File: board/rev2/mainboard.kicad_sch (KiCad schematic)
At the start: 0 parts

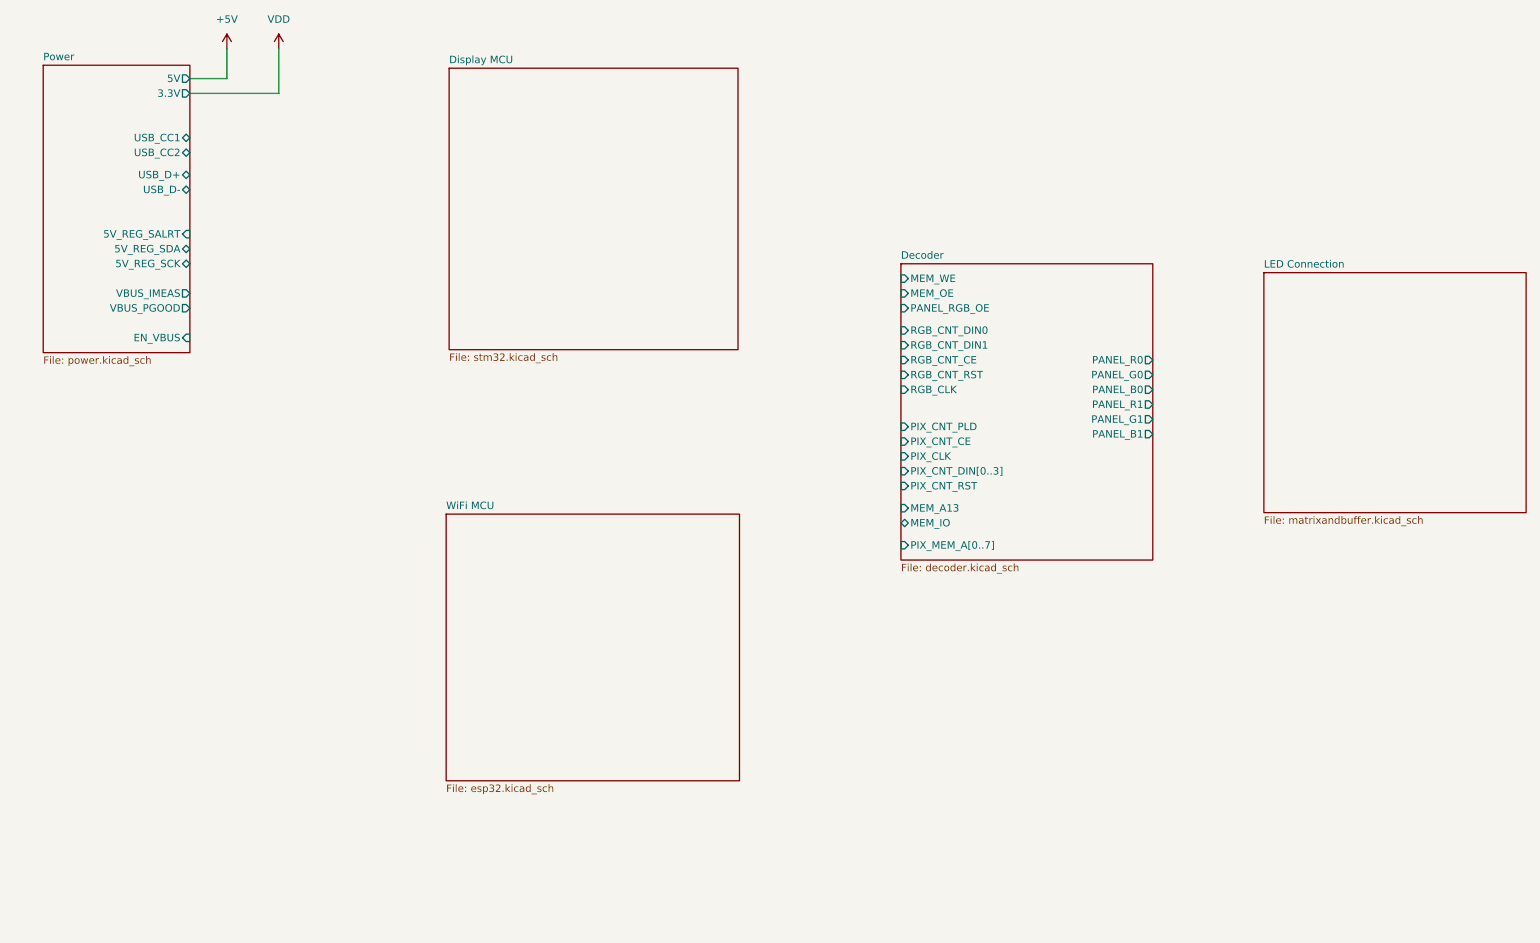
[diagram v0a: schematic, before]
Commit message: Continue board work
- move to rp2040, separate stm32g071 to do usb-c + aux ctrl IO
  - still cheaper lol with the cost of stm32s
- more power reg stuff
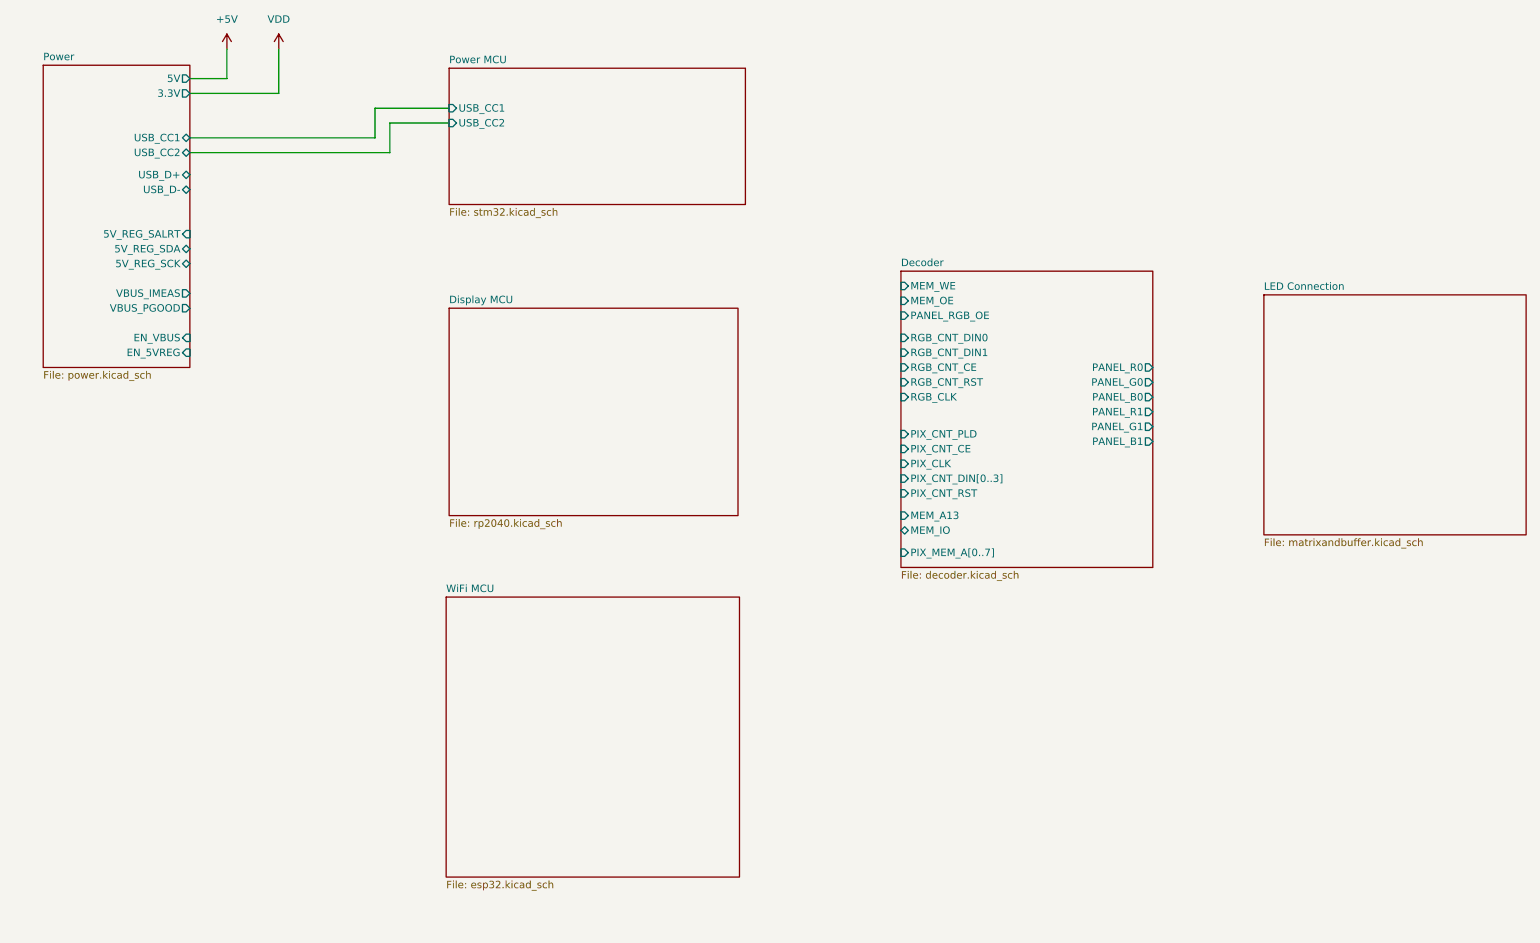
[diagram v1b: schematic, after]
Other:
- added sheet Power MCU (stm32.kicad_sch)
- sheet Display MCU: file stm32.kicad_sch -> rp2040.kicad_sch
- sheet Power ports: added EN_5VREG; removed none
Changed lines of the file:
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@@
+	(wire
+		(pts
+			(xy 80.01 39.37) (xy 45.72 39.37)
+		)
+		(stroke
+			(width 0)
+			(type default)
+		)
+	)
+	(wire
+		(pts
+			(xy 77.47 36.83) (xy 77.47 31.75)
+		)
+		(stroke
+			(width 0)
+			(type default)
+		)
+	)
 	(wire
 		(pts
@@
 	(wire
 		(pts
+			(xy 77.47 31.75) (xy 90.17 31.75)
+		)
+		(stroke
+			(width 0)
+			(type default)
+		)
+	)
+	(wire
+		(pts
 			(xy 45.72 26.67) (xy 52.07 26.67)
 		)
@@
 	(wire
 		(pts
+			(xy 90.17 34.29) (xy 80.01 34.29)
+		)
+		(stroke
+			(width 0)
+			(type default)
+		)
+	)
+	(wire
+		(pts
 			(xy 52.07 26.67) (xy 52.07 21.59)
+		)
+		(stroke
+			(width 0)
+			(type default)
+		)
+	)
+	(wire
+		(pts
+			(xy 45.72 36.83) (xy 77.47 36.83)
+		)
+		(stroke
+			(width 0)
+			(type default)
+		)
+	)
+	(wire
+		(pts
+			(xy 80.01 34.29) (xy 80.01 39.37)
 		)
 		(stroke
@@
 	)
 	(sheet
-		(at 167.64 58.42)
+		(at 90.17 66.04)
+		(size 49.53 35.56)
+		(exclude_from_sim no)
+		(in_bom yes)
+		(on_board yes)
+		(dnp no)
+		(fields_autoplaced yes)
+		(stroke
+			(width 0.1524)
+			(type solid)
+		)
+		(fill
+			(color 0 0 0 0.0000)
+		)
+		(property "Sheetname" "Display MCU"
+			(at 90.17 65.3284 0)
+			(effects
+				(font
+					(size 1.27 1.27)
+				)
+				(justify left bottom)
+			)
+		)
+		(property "Sheetfile" "rp2040.kicad_sch"
+			(at 90.17 102.1846 0)
+			(effects
+				(font
+					(size 1.27 1.27)
+				)
+				(justify left top)
+			)
+		)
+		(instances
+			(project "mainboard"
+				(path "/32eb05c7-b4a6-42f3-8fb3-43453631100f"
+					(page "7")
+				)
+			)
+		)
+	)
+	(sheet
+		(at 167.64 59.69)
 		(size 43.18 50.8)
 		(exclude_from_sim no)
@@
 		)
 		(property "Sheetname" "Decoder"
-			(at 167.64 57.7084 0)
+			(at 167.64 58.9784 0)
 			(effects
 				(font
@@
 		)
 		(property "Sheetfile" "decoder.kicad_sch"
-			(at 167.64 109.8046 0)
+			(at 167.64 111.0746 0)
 			(effects
 				(font
@@
 		)
 		(pin "MEM_WE" input
-			(at 167.64 60.96 180)
+			(at 167.64 62.23 180)
 			(effects
 				(font
@@
 		)
 		(pin "MEM_OE" input
-			(at 167.64 63.5 180)
+			(at 167.64 64.77 180)
 			(effects
 				(font
@@
 		)
 		(pin "PANEL_RGB_OE" input
-			(at 167.64 66.04 180)
+			(at 167.64 67.31 180)
 			(effects
 				(font
@@
 		)
 		(pin "RGB_CNT_DIN0" input
-			(at 167.64 69.85 180)
+			(at 167.64 71.12 180)
 			(effects
 				(font
@@
 		)
 		(pin "RGB_CNT_DIN1" input
-			(at 167.64 72.39 180)
+			(at 167.64 73.66 180)
 			(effects
 				(font
@@
 		)
 		(pin "RGB_CNT_CE" input
-			(at 167.64 74.93 180)
+			(at 167.64 76.2 180)
 			(effects
 				(font
@@
 		)
 		(pin "RGB_CNT_RST" input
-			(at 167.64 77.47 180)
+			(at 167.64 78.74 180)
 			(effects
 				(font
@@
 		)
 		(pin "RGB_CLK" input
-			(at 167.64 80.01 180)
+			(at 167.64 81.28 180)
 			(effects
 				(font
@@
 		)
 		(pin "PIX_CNT_PLD" input
-			(at 167.64 86.36 180)
+			(at 167.64 87.63 180)
 			(effects
 				(font
@@
 		)
 		(pin "PIX_CNT_CE" input
-			(at 167.64 88.9 180)
+			(at 167.64 90.17 180)
 			(effects
 				(font
@@
 		)
 		(pin "PIX_CLK" input
-			(at 167.64 91.44 180)
+			(at 167.64 92.71 180)
 			(effects
 				(font
@@
 		)
 		(pin "PIX_CNT_DIN[0..3]" input
-			(at 167.64 93.98 180)
+			(at 167.64 95.25 180)
 			(effects
 				(font
@@
 		)
 		(pin "PIX_CNT_RST" input
-			(at 167.64 96.52 180)
+			(at 167.64 97.79 180)
 			(effects
 				(font
@@
 		)
 		(pin "PANEL_B1" output
-			(at 210.82 87.63 0)
+			(at 210.82 88.9 0)
 			(effects
 				(font
@@
 		)
 		(pin "PANEL_G0" output
-			(at 210.82 77.47 0)
+			(at 210.82 78.74 0)
 			(effects
 				(font
@@
 		)
 		(pin "PANEL_R0" output
-			(at 210.82 74.93 0)
+			(at 210.82 76.2 0)
 			(effects
 				(font
@@
 		)
 		(pin "PANEL_G1" output
-			(at 210.82 85.09 0)
+			(at 210.82 86.36 0)
 			(effects
 				(font
@@
 		)
 		(pin "PANEL_R1" output
-			(at 210.82 82.55 0)
+			(at 210.82 83.82 0)
 			(effects
 				(font
@@
 		)
 		(pin "PANEL_B0" output
-			(at 210.82 80.01 0)
+			(at 210.82 81.28 0)
 			(effects
 				(font
@@
 		)
 		(pin "MEM_A13" input
-			(at 167.64 100.33 180)
+			(at 167.64 101.6 180)
 			(effects
 				(font
@@
 		)
 		(pin "MEM_IO" bidirectional
-			(at 167.64 102.87 180)
+			(at 167.64 104.14 180)
 			(effects
 				(font
@@
 		)
 		(pin "PIX_MEM_A[0..7]" input
-			(at 167.64 106.68 180)
+			(at 167.64 107.95 180)
 			(effects
 				(font
@@
 	(sheet
 		(at 90.17 24.892)
-		(size 49.53 48.26)
+		(size 50.8 23.368)
 		(exclude_from_sim no)
 		(in_bom yes)
@@
 			(color 0 0 0 0.0000)
 		)
-		(property "Sheetname" "Display MCU"
+		(property "Sheetname" "Power MCU"
 			(at 90.17 24.1804 0)
 			(effects
@@
 		)
 		(property "Sheetfile" "stm32.kicad_sch"
-			(at 90.17 73.7366 0)
+			(at 90.17 48.8446 0)
 			(effects
 				(font
@@
 				)
 				(justify left top)
+			)
+		)
+		(pin "USB_CC1" input
+			(at 90.17 31.75 180)
+			(effects
+				(font
+					(size 1.27 1.27)
+				)
+				(justify left)
+			)
+		)
+		(pin "USB_CC2" input
+			(at 90.17 34.29 180)
+			(effects
+				(font
+					(size 1.27 1.27)
+				)
+				(justify left)
 			)
 		)
@@
 	(sheet
 		(at 20.574 24.384)
-		(size 25.146 49.276)
+		(size 25.146 51.816)
 		(exclude_from_sim no)
 		(in_bom yes)
@@
 		)
 		(property "Sheetfile" "power.kicad_sch"
-			(at 20.574 74.2446 0)
+			(at 20.574 76.7846 0)
 			(effects
 				(font
@@
 		(pin "VBUS_PGOOD" output
 			(at 45.72 66.04 0)
+			(effects
+				(font
+					(size 1.27 1.27)
+				)
+				(justify right)
+			)
+		)
+		(pin "EN_5VREG" input
+			(at 45.72 73.66 0)
 			(effects
 				(font
@@
 	)
 	(sheet
-		(at 89.662 101.346)
-		(size 50.292 45.72)
+		(at 89.662 115.57)
+		(size 50.292 48.006)
 		(exclude_from_sim no)
 		(in_bom yes)
@@
 		)
 		(property "Sheetname" "WiFi MCU"
-			(at 89.662 100.6344 0)
+			(at 89.662 114.8584 0)
 			(effects
 				(font
@@
 		)
 		(property "Sheetfile" "esp32.kicad_sch"
-			(at 89.662 147.6506 0)
+			(at 89.662 164.1606 0)
 			(effects
 				(font
@@
 	)
 	(sheet
-		(at 229.87 59.944)
+		(at 229.87 63.754)
 		(size 44.958 41.148)
 		(exclude_from_sim no)
@@
 		)
 		(property "Sheetname" "LED Connection"
-			(at 229.87 59.2324 0)
+			(at 229.87 63.0424 0)
 			(effects
 				(font
@@
 		)
 		(property "Sheetfile" "matrixandbuffer.kicad_sch"
-			(at 229.87 101.6766 0)
+			(at 229.87 105.4866 0)
 			(effects
 				(font
@@
 			(project "mainboard"
 				(path "/32eb05c7-b4a6-42f3-8fb3-43453631100f"
-					(page "7")
-				)
-			)
+					(page "9")
+				)
+			)

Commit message: Split out board into A/B
allow 2x displays (for chaining)
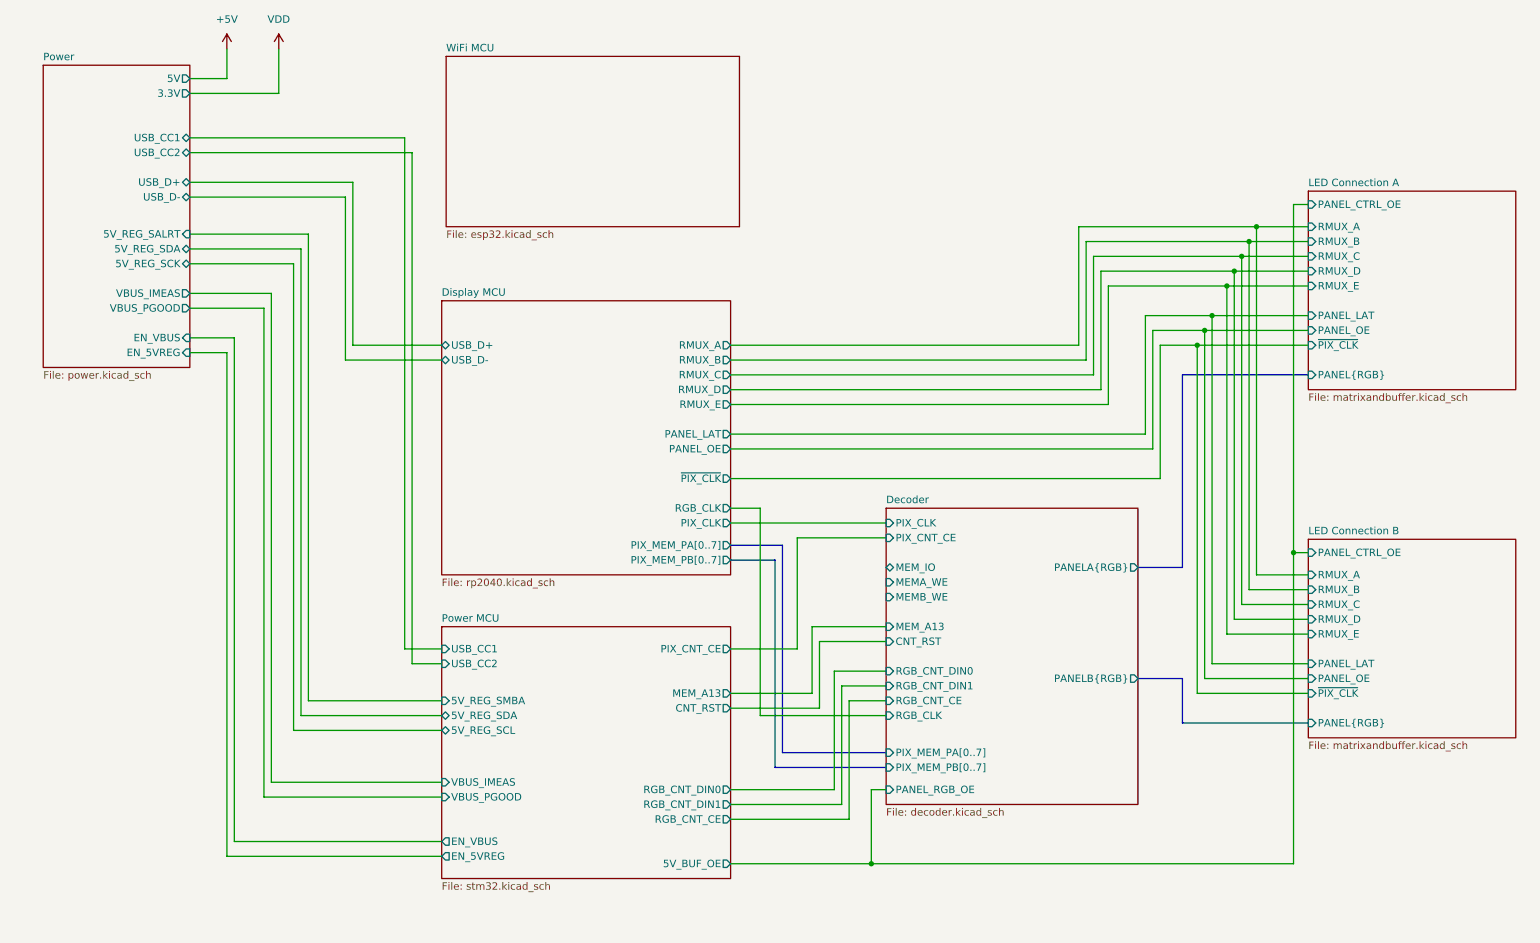
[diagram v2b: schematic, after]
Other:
- sheet LED Connection renamed LED Connection A
- added sheet LED Connection B (matrixandbuffer.kicad_sch)
- sheet Decoder ports: added CNT_RST, MEMA_WE, MEMB_WE, PANELA{RGB}, PANELB{RGB}, PIX_MEM_PA[0..7], PIX_MEM_PB[0..7]; removed MEM_OE, MEM_WE, PANEL_B0, PANEL_B1, PANEL_G0, PANEL_G1, PANEL_R0, PANEL_R1, PIX_CNT_DIN[0..3], PIX_CNT_PLD, PIX_CNT_RST, PIX_MEM_A[0..7], RGB_CNT_RST
- sheet Display MCU ports: added PANEL_LAT, PANEL_OE, PIX_CLK, PIX_MEM_PA[0..7], PIX_MEM_PB[0..7], RGB_CLK, RMUX_A, RMUX_B, RMUX_C, RMUX_D, RMUX_E, USB_D+, USB_D-, ~{PIX_CLK}; removed none
- sheet LED Connection A ports: added PANEL_CTRL_OE, PANEL_LAT, PANEL_OE, PANEL{RGB}, RMUX_A, RMUX_B, RMUX_C, RMUX_D, RMUX_E, ~{PIX_CLK}; removed none
- sheet Power MCU ports: added 5V_BUF_OE, 5V_REG_SCL, 5V_REG_SDA, 5V_REG_SMBA, CNT_RST, EN_5VREG, EN_VBUS, MEM_A13, PIX_CNT_CE, RGB_CNT_CE, RGB_CNT_DIN0, RGB_CNT_DIN1, VBUS_IMEAS, VBUS_PGOOD; removed none

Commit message: More board work
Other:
- added sheet Peripherals (peripherals.kicad_sch)
- sheet Decoder ports: added PIX_CNT_DIN[0..3], PIX_CNT_PE; removed none
- sheet Display MCU ports: added PIX_CNT_DIN[0..3]; removed none
- sheet Power MCU ports: added COMM0{TX RX}, COMM1{TX RX}, PIX_CNT_PE; removed none
